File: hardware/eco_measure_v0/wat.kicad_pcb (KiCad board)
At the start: 2 copper layers, 67.2 x 86.2 mm, 32 parts, among them J4 Conn_02x05_Odd_Even, P1 V_IN, P2 PINZA_1, P3 PINZA_2, P4 PINZA_3, P5 PINZA_4, P6 PINZA_5, P7 PINZA_6, P8 PINZA_7, U1 LM358, U2 NANO

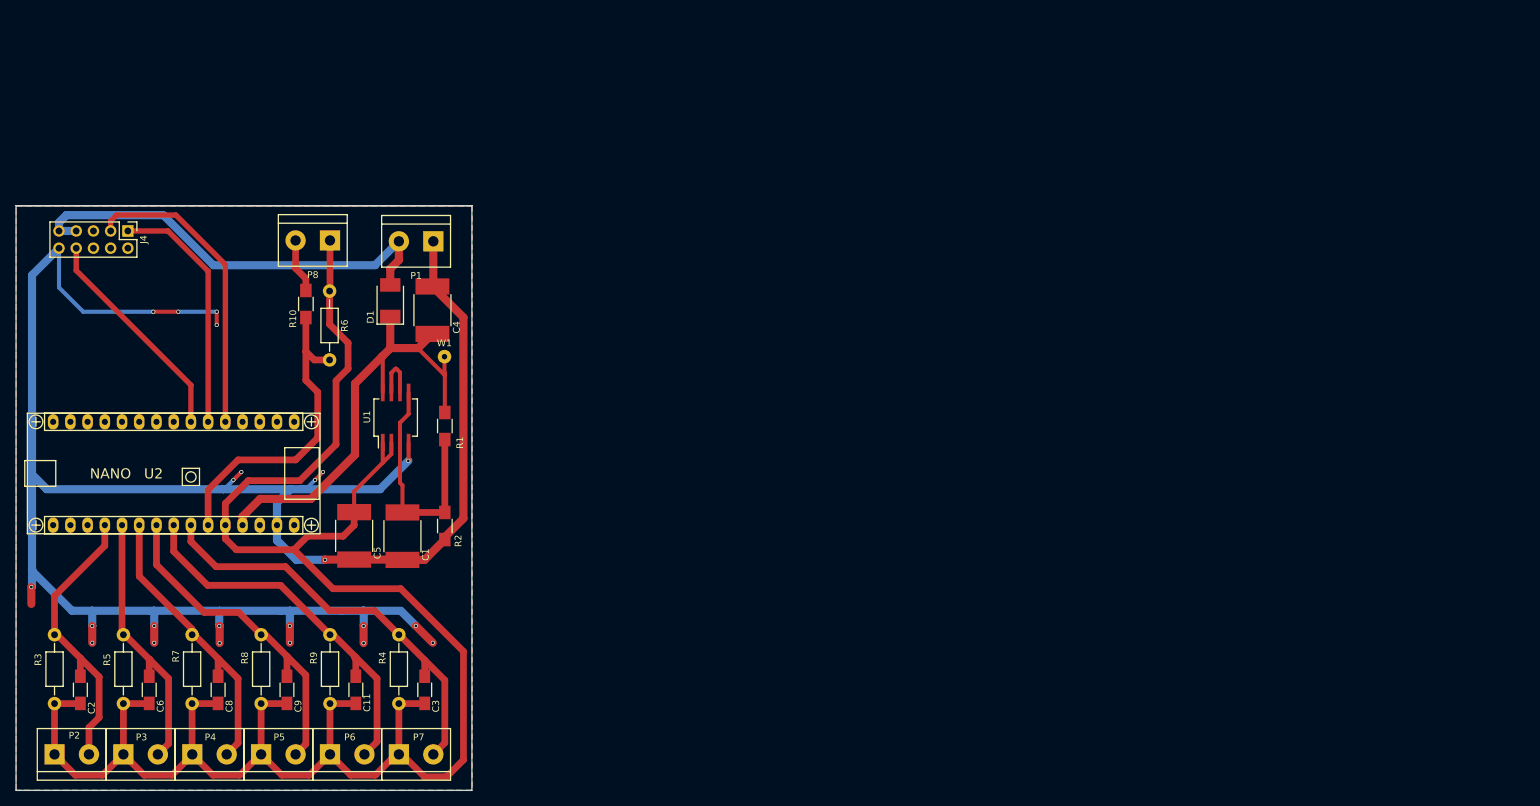
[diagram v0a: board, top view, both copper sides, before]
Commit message: avanzando en la medida continua y la PCB
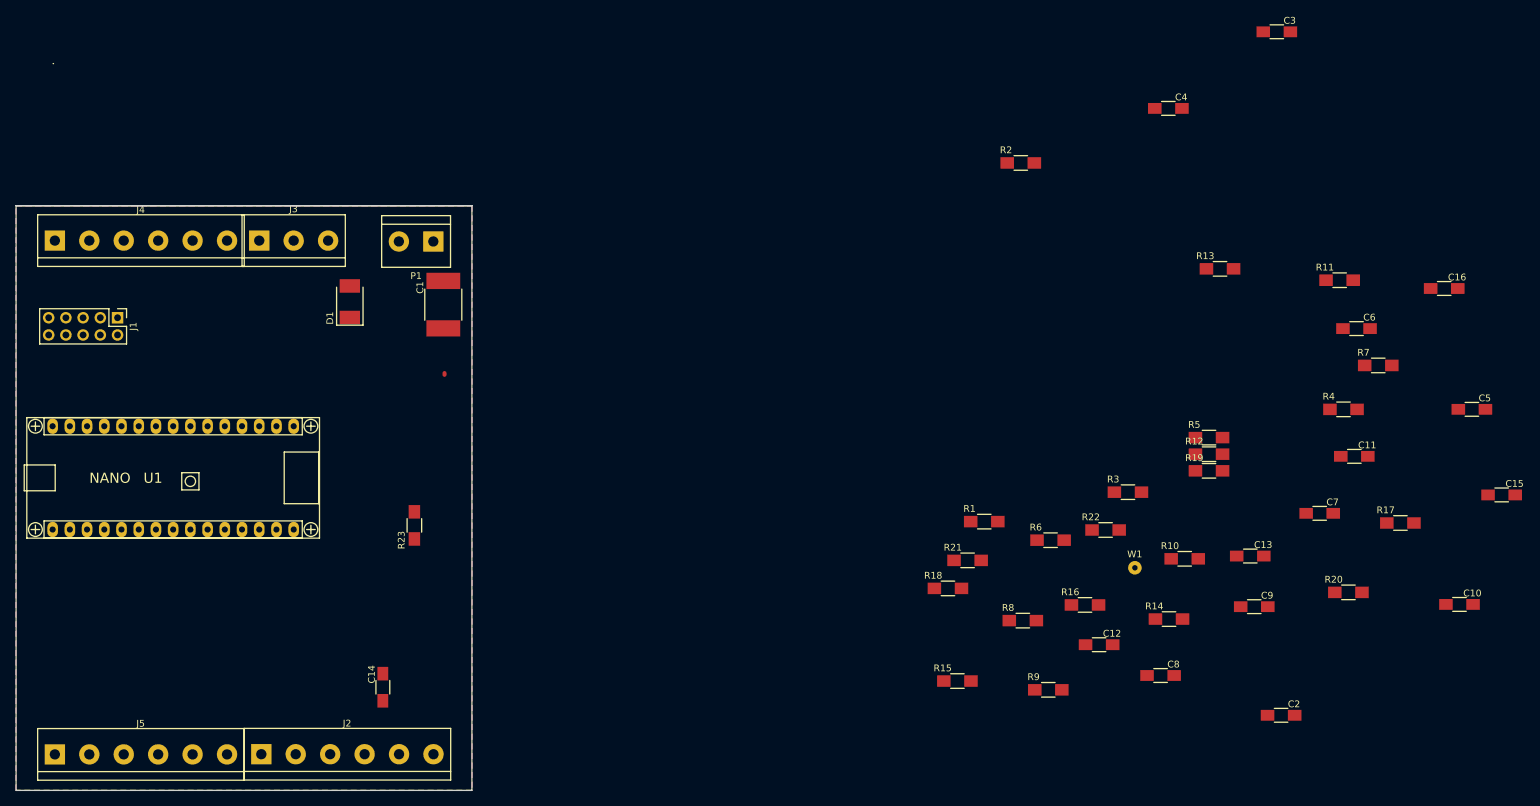
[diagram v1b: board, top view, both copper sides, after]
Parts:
- removed P2: PINZA_1, Connectors_Terminal_Blocks:TerminalBlock_bornier-2_P5.08mm
- removed P3: PINZA_2, Connectors_Terminal_Blocks:TerminalBlock_bornier-2_P5.08mm
- removed P4: PINZA_3, Connectors_Terminal_Blocks:TerminalBlock_bornier-2_P5.08mm
- removed P5: PINZA_4, Connectors_Terminal_Blocks:TerminalBlock_bornier-2_P5.08mm
- removed P6: PINZA_5, Connectors_Terminal_Blocks:TerminalBlock_bornier-2_P5.08mm
- removed P7: PINZA_6, Connectors_Terminal_Blocks:TerminalBlock_bornier-2_P5.08mm
- removed P8: PINZA_7, Connectors_Terminal_Blocks:TerminalBlock_bornier-2_P5.08mm
- removed U2: NANO, libreria_huellas_proyecto:arduino_nano
- added C10: 100nF, eco_power_v2:C_1206_HandSoldering, F.Cu at (273.7, 132.8)
- added C12: 100nF, eco_power_v2:C_1206_HandSoldering, F.Cu at (220.5, 138.8)
- added C13: 100nF, eco_power_v2:C_1206_HandSoldering, F.Cu at (242.8, 125.7)
- added C14: 100nF, eco_power_v2:C_1206_HandSoldering, F.Cu at (114.9, 145.0)
- added C15: 100nF, eco_power_v2:C_1206_HandSoldering, F.Cu at (279.9, 116.7)
- added C16: 100nF, eco_power_v2:C_1206_HandSoldering, F.Cu at (271.4, 86.2)
- added C7: 100nF, eco_power_v2:C_1206_HandSoldering, F.Cu at (253.1, 119.4)
- added J1: Conn_02x05_Odd_Even, eco_power_v2:Pin_Header_Straight_2x05_Pitch2.54mm_onsar, F.Cu at (75.7, 90.5)
- added J2: Conn_01x06, TerminalBlock:TerminalBlock_bornier-6_P5.08mm, F.Cu at (96.9, 154.9)
- added J3: Conn_01x03, TerminalBlock:TerminalBlock_bornier-3_P5.08mm, F.Cu at (96.6, 79.1)
- added J5: Conn_01x06, TerminalBlock:TerminalBlock_bornier-6_P5.08mm, F.Cu at (66.5, 154.9)
- added R11: 10k, eco_power_v2:R_1206_HandSoldering, F.Cu at (256.0, 85.0)
- added R12: 10k, eco_power_v2:R_1206_HandSoldering, F.Cu at (236.7, 110.7)
- added R13: 10k, eco_power_v2:R_1206_HandSoldering, F.Cu at (238.4, 83.3)
- added R14: 10k, eco_power_v2:R_1206_HandSoldering, F.Cu at (230.8, 135.0)
- added R15: 10k, eco_power_v2:R_1206_HandSoldering, F.Cu at (199.6, 144.1)
- added R16: 10k, eco_power_v2:R_1206_HandSoldering, F.Cu at (218.4, 132.9)
- added R17: 10k, eco_power_v2:R_1206_HandSoldering, F.Cu at (265.0, 120.8)
- added R18: 10k, eco_power_v2:R_1206_HandSoldering, F.Cu at (198.2, 130.5)
- added R19: 10k, eco_power_v2:R_1206_HandSoldering, F.Cu at (236.7, 113.1)
- added R20: 10k, eco_power_v2:R_1206_HandSoldering, F.Cu at (257.3, 131.0)
- added R21: 10k, eco_power_v2:R_1206_HandSoldering, F.Cu at (201.1, 126.3)
- added R22: 10k, eco_power_v2:R_1206_HandSoldering, F.Cu at (221.5, 121.8)
- added R23: 10k, eco_power_v2:R_1206_HandSoldering, F.Cu at (119.5, 121.2)
- C1: footprint Capacitors_SMD:C_2220_HandSoldering -> eco_power_v2:C_2220_HandSoldering
- C11, C2, C3, C6, C8, C9: footprint Capacitors_SMD:C_1206_HandSoldering -> eco_power_v2:C_1206_HandSoldering
- C4, C5: value 10uF -> 100nF; footprint Capacitors_SMD:C_2220_HandSoldering -> eco_power_v2:C_1206_HandSoldering
- D1: footprint Diodes_SMD:D_2114 -> eco_power_v2:D_2114
- J4: value Conn_02x05_Odd_Even -> Conn_01x06; footprint oscar_libreria_huellas:Pin_Header_Straight_2x05_Pitch2.54mm_onsar -> TerminalBlock:TerminalBlock_bornier-6_P5.08mm
- P1: footprint Connectors_Terminal_Blocks:TerminalBlock_bornier-2_P5.08mm -> eco_power_v2:TerminalBlock_bornier-2_P5.08mm
- R1, R2: value 4K7 -> 10k; footprint Resistors_SMD:R_1206_HandSoldering -> eco_power_v2:R_1206_HandSoldering
- R10: footprint Resistors_SMD:R_1206_HandSoldering -> eco_power_v2:R_1206_HandSoldering
- R3, R4, R5, R7, R8, R9: footprint libreria_huellas_proyecto:Resistor_Horizontal_RM10mm -> eco_power_v2:R_1206_HandSoldering
- R6: value 1k -> 10k; footprint libreria_huellas_proyecto:Resistor_Horizontal_RM10mm -> eco_power_v2:R_1206_HandSoldering
- U1: value LM358 -> NANO; footprint Housings_SOIC:SO-8_5.3x6.2mm_Pitch1.27mm -> eco_power_v2:arduino_nano
- W1: footprint Wire_Pads:SolderWirePad_single_0-8mmDrill -> eco_power_v2:SolderWirePad_single_0-8mmDrill
- moved C6 185.9 mm to (258.5, 92.1), turned to 0 degrees
- moved R7 179.4 mm to (261.7, 97.6), turned to 0 degrees
- moved C2 177.2 mm to (247.4, 149.2), turned to 0 degrees
- moved C5 165.9 mm to (275.5, 104.0), turned to 0 degrees
- moved R5 162.8 mm to (236.7, 108.2), turned to 0 degrees
- moved R3 159.7 mm to (224.8, 116.3), turned to 0 degrees
- moved C3 158.8 mm to (246.7, 48.3), turned to 0 degrees
- moved C11 151.3 mm to (258.2, 111.0), turned to 0 degrees
- moved R4 143.3 mm to (256.6, 104.0), turned to 0 degrees
- moved C9 143.2 mm to (243.4, 133.1), turned to 0 degrees
- moved C8 139.1 mm to (229.6, 143.3), turned to 0 degrees
- moved R10 135.0 mm to (233.1, 126.1), turned to 0 degrees
- moved C4 112.6 mm to (230.7, 59.6), turned to 0 degrees
- moved R8 112.4 mm to (209.3, 135.2), turned to 0 degrees
- moved R6 109.6 mm to (213.4, 123.3), turned to 0 degrees
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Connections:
- C1 pad 1: /v_25 -> VCC
- C11 pad 1: /intensidad_5 -> /A2
- C11 pad 2: /v_referencia -> GND
- C2 pad 1: /intensidad_1 -> /D2
- C2 pad 2: /v_referencia -> GND
- C3 pad 1: /intensidad_6 -> /D3
- C3 pad 2: /v_referencia -> GND
- C4 pad 1: VCC -> /D4
- C5 pad 1: /v_referencia -> /D10
- C6 pad 1: /intensidad_2 -> /D11
- C6 pad 2: /v_referencia -> GND
- C8 pad 1: /intensidad_3 -> /D13
- C8 pad 2: /v_referencia -> GND
- C9 pad 1: /intensidad_4 -> /A0
- C9 pad 2: /v_referencia -> GND
- J4 pad 1: /ard_tx -> /vcc_5v
- J4 pad 2: Net-(J4-Pad2) -> /D13
- J4 pad 3: /ard_rx -> /D12
- J4 pad 4: Net-(J4-Pad4) -> /D11
- J4 pad 5: GND -> /D10
- J4 pad 6: Net-(J4-Pad6) -> /D4
- R1 pad 1: VCC -> /D2
- R1 pad 2: /v_25 -> VCC
- R10 pad 1: /voltage_1 -> /A2
- R10 pad 2: Net-(P8-Pad2) -> /jA2
- R2 pad 1: /v_25 -> /D3
- R2 pad 2: GND -> VCC
- R3 pad 1: /intensidad_1 -> /D4
- R3 pad 2: /v_referencia -> VCC
- R4 pad 1: /intensidad_6 -> /D10
- R4 pad 2: /v_referencia -> VCC
- R5 pad 1: /intensidad_2 -> /D11
- R5 pad 2: /v_referencia -> VCC
- R6 pad 1: /voltage_1 -> /D12
- R6 pad 2: /v_referencia -> VCC
- R7 pad 1: /intensidad_3 -> /D13
- R7 pad 2: /v_referencia -> VCC
- R8 pad 1: /intensidad_4 -> /A0
- R8 pad 2: /v_referencia -> /jA0
- R9 pad 1: /intensidad_5 -> /A1
- R9 pad 2: /v_referencia -> /jA1
- U1 pad 1: /v_referencia -> /ard_tx
- U1 pad 2: /v_referencia -> /ard_rx
- U1 pad 3: /v_25 -> Net-(U1-Pad3)
- U1 pad 5: /v_25 -> /D2
- U1 pad 6: Net-(U1-Pad6) -> /D3
- U1 pad 7: Net-(U1-Pad6) -> /D4
- U1 pad 8: VCC -> Net-(U1-Pad8)
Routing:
- net GND: track 325.2 -> 0.00 mm, vias 23 -> 0
- net /v_referencia: track 286.6 -> 0.00 mm
- net VCC: track 71.2 -> 0.27 mm
- net /vcc_5v: track 65.9 -> 0.00 mm
- net /intensidad_6: track 62.4 -> 0.00 mm
- net /intensidad_5: track 56.8 -> 0.00 mm
- net /intensidad_4: track 50.5 -> 0.00 mm
- net /voltage_1: track 47.0 -> 0.00 mm
- net /ard_rx: track 45.0 -> 0.00 mm
- net /intensidad_3: track 43.6 -> 0.00 mm
- net /intensidad_1: track 43.1 -> 0.00 mm
- net /intensidad_2: track 40.1 -> 0.00 mm
- net /ard_tx: track 36.5 -> 0.00 mm
- net /v_25: track 35.4 -> 0.00 mm
- net /ard_d4: track 32.6 -> 0.00 mm
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
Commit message: avanzando en el diseño de la pcb
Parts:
- moved C10 199.0 mm to (74.7, 129.9), turned to 180 degrees
- moved R11 181.5 mm to (85.3, 146.8), turned to 90 degrees
- moved R17 181.1 mm to (84.3, 134.3)
- moved C11 180.5 mm to (79.6, 137.6), turned to 180 degrees
- moved C9 176.7 mm to (66.8, 137.5), turned to 180 degrees
- moved R14 164.2 mm to (66.8, 141.1)
- moved C15 163.7 mm to (116.7, 129.7)
- moved C16 157.7 mm to (122.3, 137.4)
- moved R10 155.9 mm to (78.6, 146.8), turned to 270 degrees
- moved C3 153.6 mm to (98.5, 88.6)
- moved C2 152.0 mm to (105.1, 95.7)
- moved R13 143.5 mm to (109.6, 146.6), turned to 90 degrees
- moved R20 143.2 mm to (115.0, 146.5), turned to 270 degrees
- moved R8 142.4 mm to (67.4, 146.8), turned to 270 degrees
- moved C4 141.9 mm to (93.4, 95.7)
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
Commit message: sw operativo. Organizando el código
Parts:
- moved C8 161.0 mm to (69.6, 86.1)
- moved C7 152.8 mm to (73.7, 90.4), turned to 180 degrees
- moved R7 148.6 mm to (65.6, 90.4), turned to 180 degrees
- moved C6 141.5 mm to (85.9, 86.1)
- moved R6 137.4 mm to (77.7, 86.1)
- moved C5 134.7 mm to (89.9, 90.4), turned to 180 degrees
- moved R5 130.9 mm to (81.8, 90.4), turned to 180 degrees
- moved R4 119.0 mm to (94.0, 86.1)
- moved J1 48.4 mm to (75.7, 97.3)
- moved W1 23.2 mm to (139.9, 114.3)
- moved C1 17.8 mm to (120.6, 114.4)
- moved C4 12.9 mm to (102.1, 86.1)
- moved R2 12.3 mm to (110.2, 86.1)
- moved R18 8.58 mm to (98.8, 138.4)
- moved C13 8.27 mm to (98.8, 134.6), turned to 180 degrees
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
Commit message: hw version operativa completa
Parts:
- moved W1 20.6 mm to (122.9, 102.6)
- moved C1 3.18 mm to (120.5, 111.2), turned to 270 degrees
- moved D1 2.59 mm to (120.5, 95.6)
- turned R13 to 270 degrees
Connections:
- J2 pad 1: /vcc_5v -> VCC
- J4 pad 1: /vcc_5v -> VCC
- J5 pad 1: /vcc_5v -> VCC
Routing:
- net VCC: track 0.00 -> 224.4 mm, vias 0 -> 5
- net /vcc_5v: track 0.27 -> 104.1 mm
- net /ard_rx: track 0.00 -> 70.1 mm
- net /D2: track 0.00 -> 59.2 mm
- net /D3: track 0.00 -> 50.7 mm
- net /D13: track 0.00 -> 49.0 mm
- net /A7: track 0.00 -> 48.3 mm
- net /D10: track 0.00 -> 44.1 mm
- net /D4: track 0.00 -> 43.5 mm
- net /A6: track 0.00 -> 41.9 mm
- net /A5: track 0.00 -> 40.2 mm
- net /D12: track 0.00 -> 40.0 mm
- net /D11: track 0.00 -> 39.6 mm
- net /A4: track 0.00 -> 34.3 mm
- net /ard_tx: track 0.00 -> 32.3 mm
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
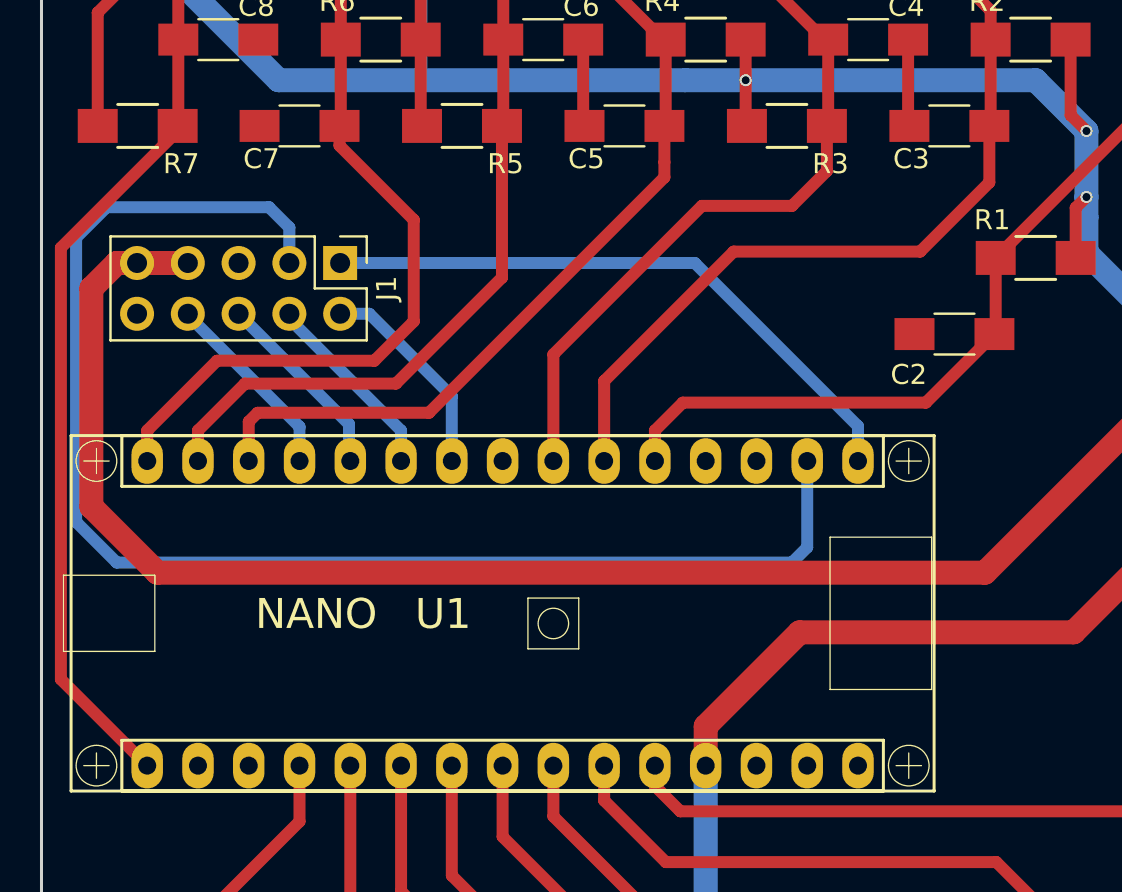
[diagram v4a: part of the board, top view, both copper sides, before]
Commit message: cambio de d13 por d5
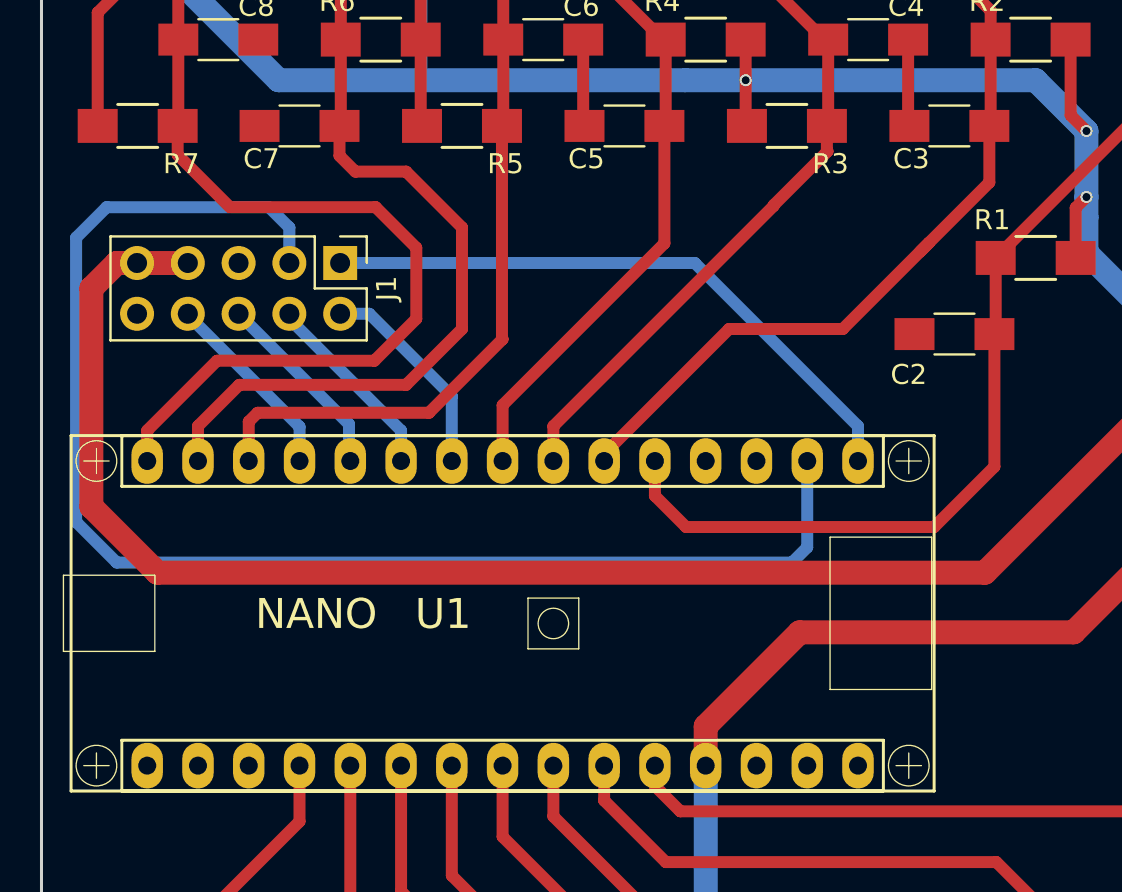
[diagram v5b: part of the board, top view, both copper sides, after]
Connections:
- C5 pad 1: /D10 -> /D5
- C6 pad 1: /D11 -> /D10
- C7 pad 1: /D12 -> /D11
- C8 pad 1: /D13 -> /D12
- J4 pad 2: /D13 -> /D12
- J4 pad 3: /D12 -> /D11
- J4 pad 4: /D11 -> /D10
- J4 pad 5: /D10 -> /D5
- R4 pad 1: /D10 -> /D5
- R5 pad 1: /D11 -> /D10
- R6 pad 1: /D12 -> /D11
- R7 pad 1: /D13 -> /D12
- U1 pad 16: /D13 -> Net-(U1-Pad16)
- U1 pad 8: Net-(U1-Pad8) -> /D5
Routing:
- net /D13: track 49.0 -> 0.00 mm
- net /D5: track 0.00 -> 34.0 mm
- net /D12: track 40.0 -> 49.0 mm
- net /D2: track 59.2 -> 65.9 mm
- net /D10: track 44.1 -> 39.2 mm
- net /D11: track 39.6 -> 42.9 mm
- net /D4: track 43.5 -> 40.9 mm
- net /D3: track 50.7 -> 49.2 mm

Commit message: PCB para fabricar
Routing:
- net /D11: track 42.9 -> 44.3 mm
- net /D10: track 39.2 -> 40.5 mm
- net /vcc_5v: track 104.1 -> 105.2 mm
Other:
- board size 67.2 x 86.2 mm -> 67.9 x 87 mm
